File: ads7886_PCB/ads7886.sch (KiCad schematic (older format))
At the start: 23 parts, among them IC1 ADS7886SDBVT, J1 2214S-08SG-85, J2 2214S-08SG-85, U1 LP5907MFX-3.3, U2 OPA355NA, U3 74LVC1G14

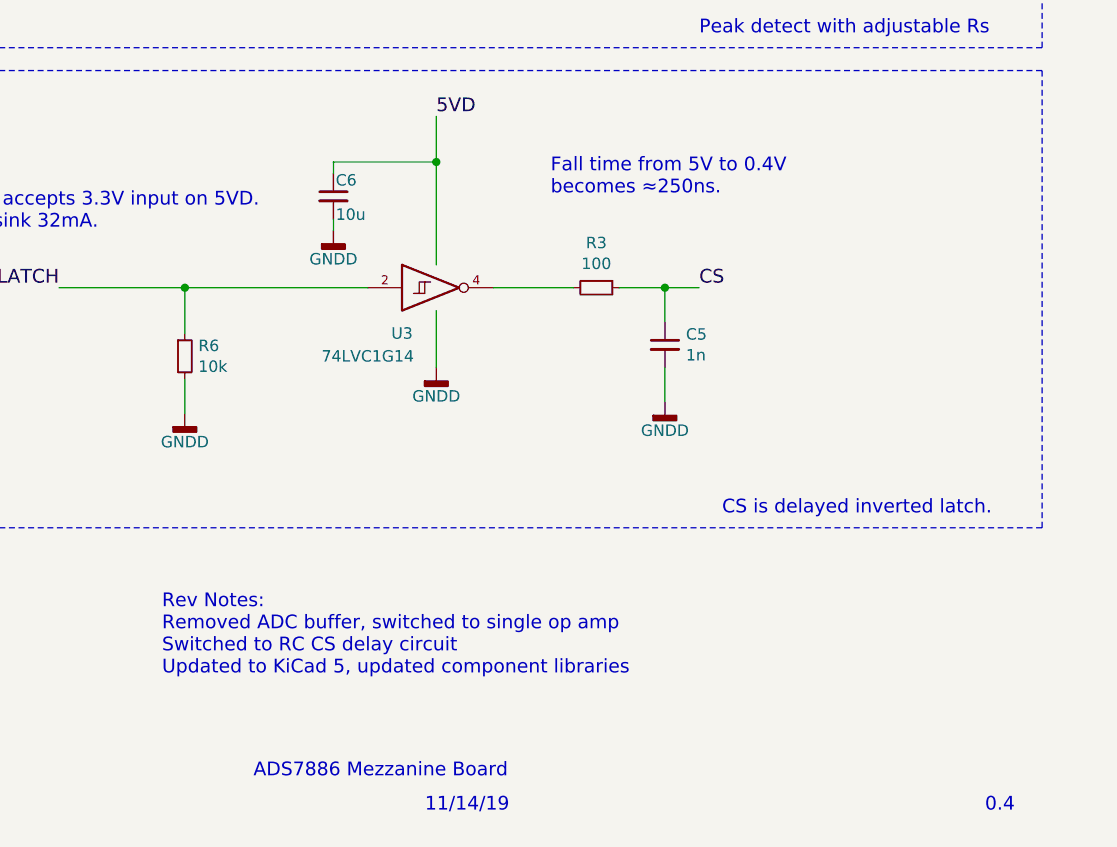
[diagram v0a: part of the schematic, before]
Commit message: Improved PCB component compatilibity
Widened LDO trace between IN and EN, mostly for aesthetics
Grounded previously NC pad on inverter to allow for optional installation of 1G240 instead of 1G14
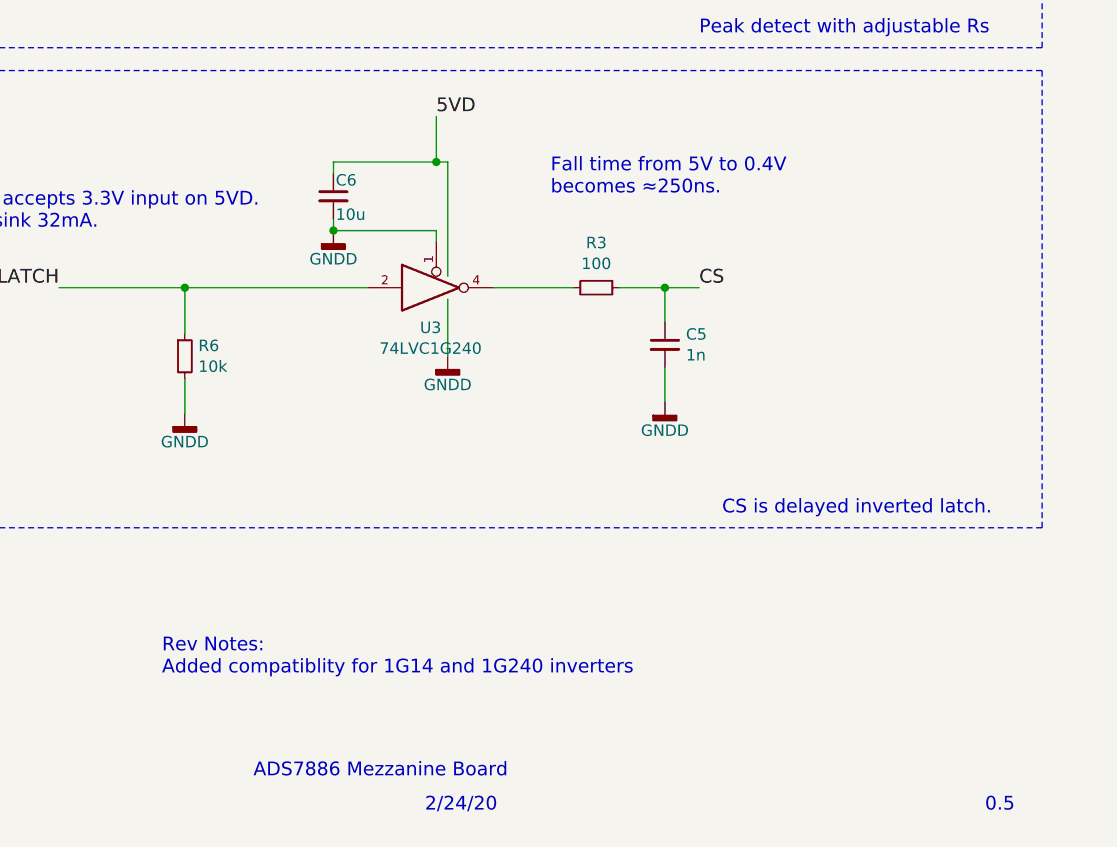
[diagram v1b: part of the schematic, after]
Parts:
- removed U3: 74LVC1G14, TO_SOT_Packages_SMD:SOT-23-5_HandSoldering, symbol 74xGxx:74LVC1G14
- added U3: 74LVC1G240, TO_SOT_Packages_SMD:SOT-23-5_HandSoldering, symbol 74xGxx:74LVC1G240
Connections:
- net GND: now also U3.1, U3.3 (GND)
- net LATCH: now also U3.2
- net VCC: now also U3.5 (VCC)
- net at R3.2: now also U3.4
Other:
- note added: "0.5"
- note added: "2/24/20"
- note added: "Rev Notes:\nAdded compatiblity for 1G14 and 1G240 inverters"
- note removed: "0.4"
- note removed: "11/14/19"
- note removed: "Rev Notes:\nRemoved ADC buffer, switched to single op amp\nSwitched to RC CS delay circuit\nUpdated to KiCad 5, updated component libraries"
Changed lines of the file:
@@
 Test Points
 Text Notes 8150 7650 0    60   ~ 0
-11/14/19
+2/24/20
 Text Notes 10600 7650 0    60   ~ 0
-0.4
+0.5
 $Comp
 L Device:C_Small C2
@@
 5VD
 Text Notes 7000 7050 0    60   ~ 0
-Rev Notes:\nRemoved ADC buffer, switched to single op amp\nSwitched to RC CS delay circuit\nUpdated to KiCad 5, updated component libraries
+Rev Notes:\nAdded compatiblity for 1G14 and 1G240 inverters
 Text Notes 5750 4550 0    60   ~ 0
 CS TIMING
@@
 Wire Wire Line
 	8200 4600 8200 4800
-Connection ~ 8200 4800
-Wire Wire Line
-	8200 5250 8200 4800
-Wire Wire Line
-	8200 5700 8200 5450
-$Comp
-L 74xGxx:74LVC1G14 U3
-U 1 1 5DE14786
-P 8200 5350
-F 0 "U3" H 8050 5150 50  0000 C CNN
-F 1 "74LVC1G14" H 7900 5050 50  0000 C CNN
-F 2 "TO_SOT_Packages_SMD:SOT-23-5_HandSoldering" H 8200 5350 50  0001 C CNN
-F 3 "http://www.ti.com/lit/sg/scyt129e/scyt129e.pdf" H 8200 5350 50  0001 C CNN
-	1    8200 5350
-	1    0    0    -1
-$EndComp
+Wire Wire Line
+	8250 5650 8250 5400
 Wire Wire Line
 	7100 5350 7900 5350
@@
 L power:GNDD #PWR011
 U 1 1 5DC22043
-P 8200 5700
-F 0 "#PWR011" H 8200 5450 50  0001 C CNN
-F 1 "GNDD" H 8200 5575 50  0000 C CNN
-F 2 "" H 8200 5700 50  0001 C CNN
-F 3 "" H 8200 5700 50  0001 C CNN
-	1    8200 5700
+P 8250 5650
+F 0 "#PWR011" H 8250 5400 50  0001 C CNN
+F 1 "GNDD" H 8250 5525 50  0000 C CNN
+F 2 "" H 8250 5650 50  0001 C CNN
+F 3 "" H 8250 5650 50  0001 C CNN
+	1    8250 5650
 	1    0    0    -1
 $EndComp
@@
 	2250 3250 2500 3250
 Connection ~ 2500 3250
+$Comp
+L 74xGxx:74LVC1G240 U3
+U 1 1 5E5503CE
+P 8200 5350
+F 0 "U3" H 8175 5175 50  0000 C CNN
+F 1 "74LVC1G240" H 8175 5084 50  0000 C CNN
+F 2 "TO_SOT_Packages_SMD:SOT-23-5_HandSoldering" H 8200 5350 50  0001 C CNN
+F 3 "http://www.ti.com/lit/sg/scyt129e/scyt129e.pdf" H 8200 5350 50  0001 C CNN
+	1    8200 5350
+	1    0    0    -1
+$EndComp
+Wire Wire Line
+	8200 4800 8250 4800
+Wire Wire Line
+	8250 4800 8250 5300
+Connection ~ 8200 4800
+Wire Wire Line
+	8200 5150 8200 5100
+Wire Wire Line
+	8200 5100 7750 5100
+Connection ~ 7750 5100
 $EndSCHEMATC
